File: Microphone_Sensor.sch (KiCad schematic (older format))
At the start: 29 parts, among them J4 Mic_Conn, U4 MAX4063

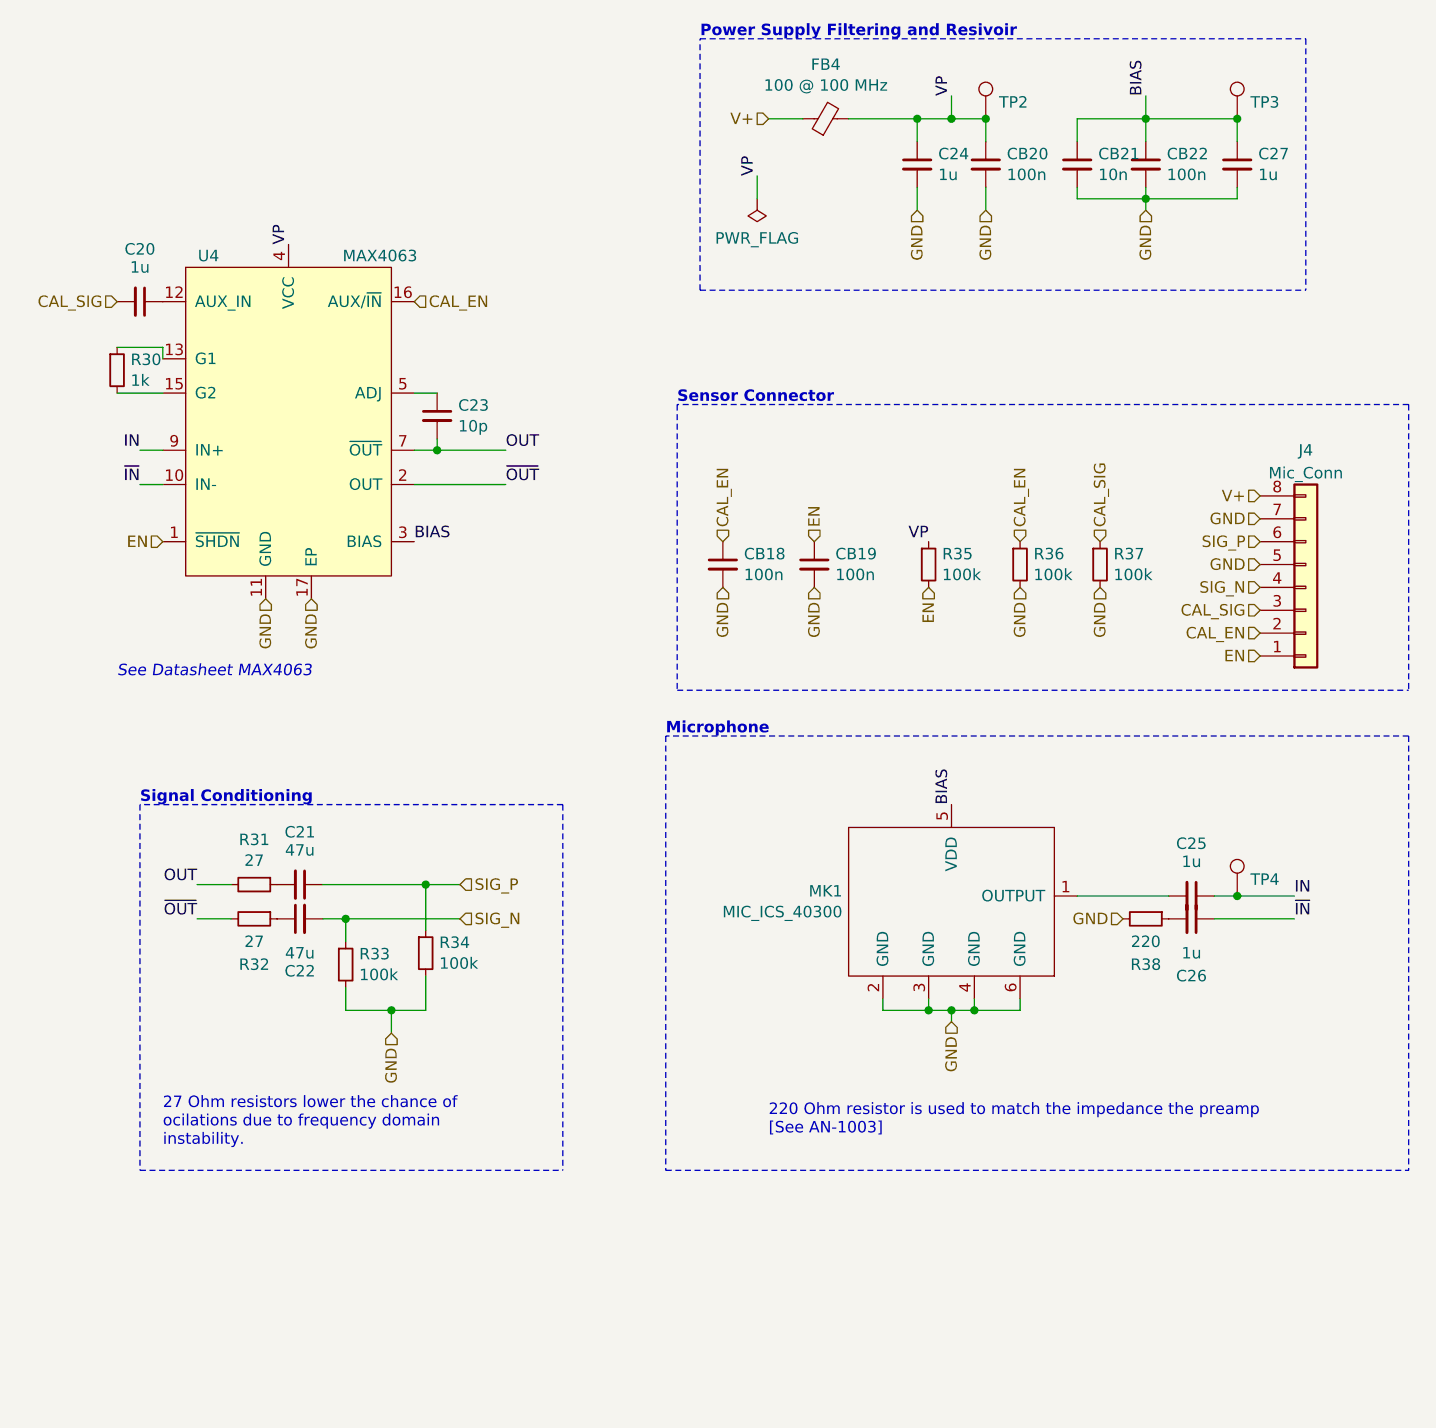
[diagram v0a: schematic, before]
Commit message: Change Sensor Connectors
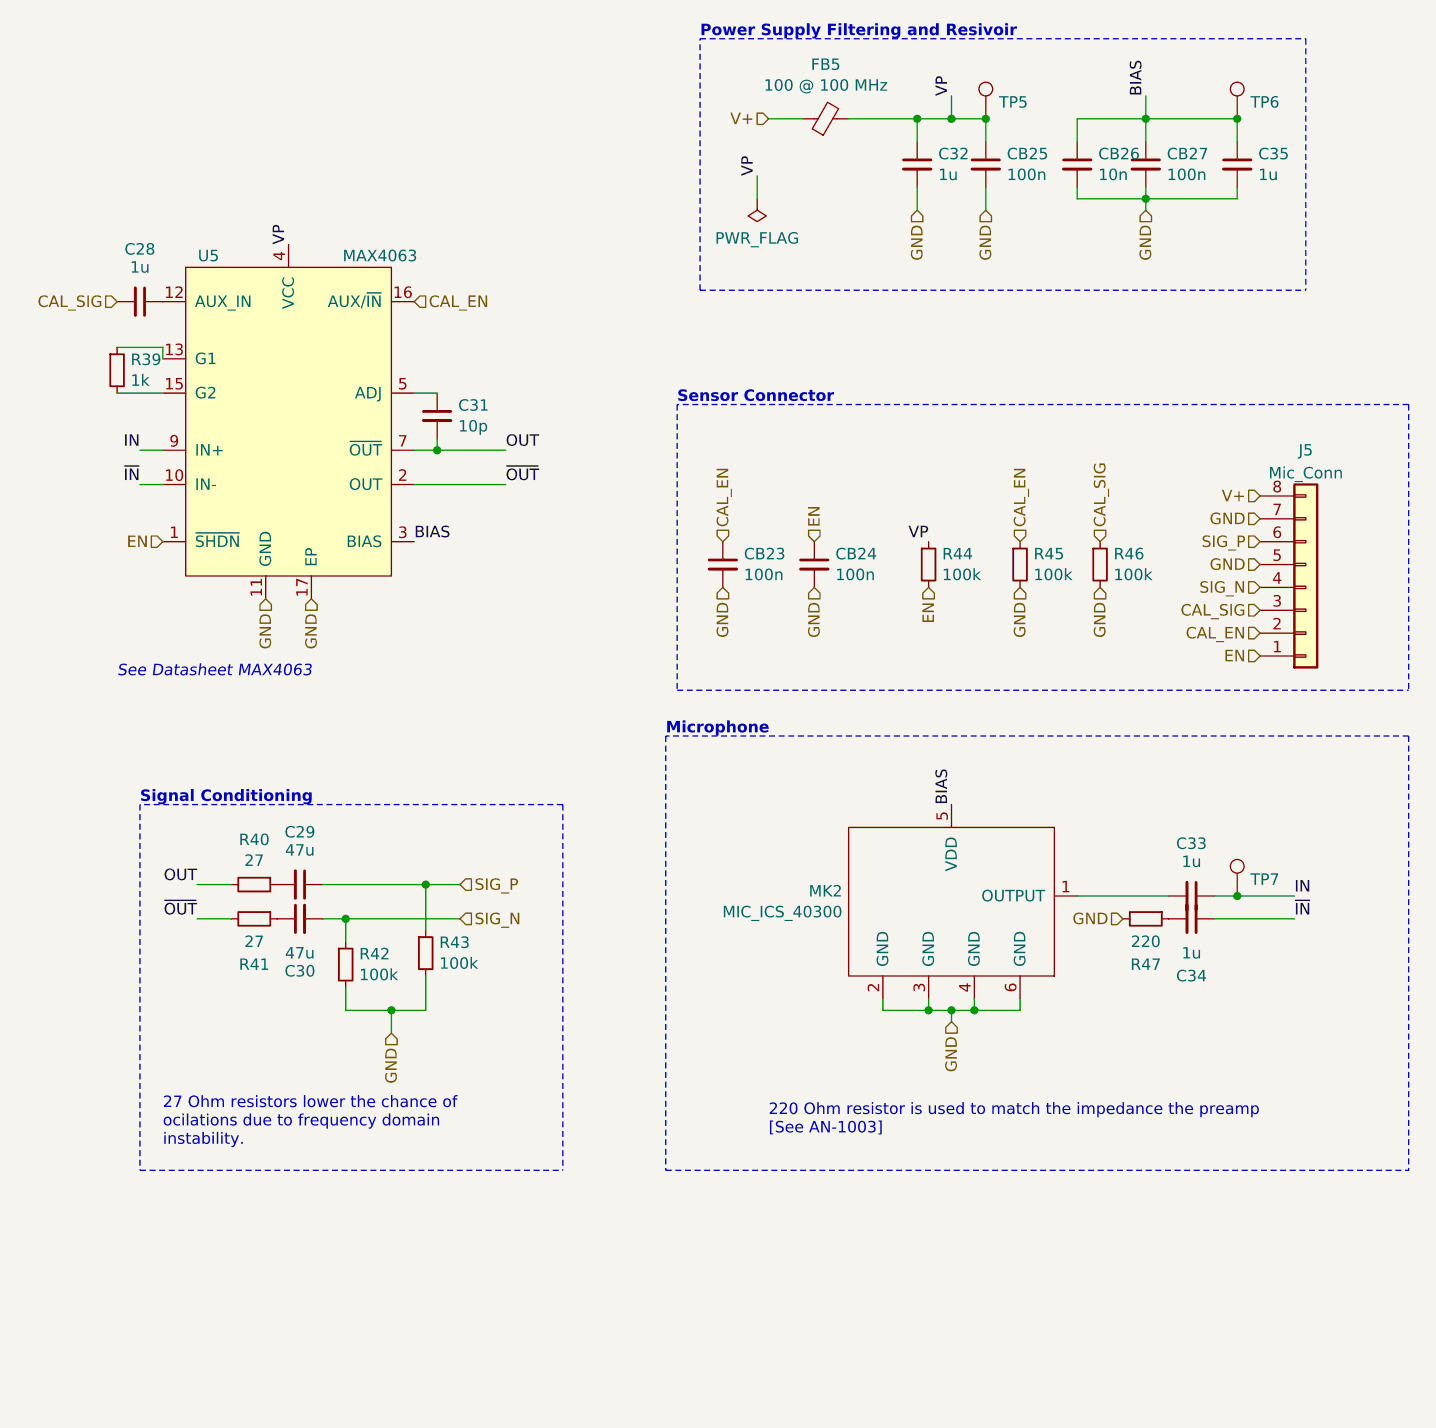
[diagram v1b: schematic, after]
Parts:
- J4: footprint Connector_Molex:Molex_PicoBlade_53047-0810_1x08_P1.25mm_Vertical -> (none); MPN 53047-0810 -> (none); Mfr. Molex -> (none)

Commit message: Setup PCB
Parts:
- J4: footprint (none) -> Connector_PinHeader_2.54mm:PinHeader_1x08_P2.54mm_Vertical
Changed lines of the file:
@@
 $Descr A4 11693 8268
 encoding utf-8
-Sheet 12 17
+Sheet 13 17
 Title "Kleinvoet"
 Date "2020-06-11"
@@
 AR Path="/5EE5ECAD/5F0013E5/5EEDE2AE" Ref="MK3"  Part="1"
 AR Path="/5EE5ECAD/5F0090C7/5EEDE2AE" Ref="MK4"  Part="1"
-F 0 "MK2" H 6123 4871 50  0000 R CNN
+F 0 "MK4" H 6123 4871 50  0000 R CNN
 F 1 "MIC_ICS_40300" H 6123 4780 50  0000 R CNN
 F 2 "grootvoet:MEMS_Mic_ICS-40300" H 6600 4750 50  0001 C CNN
@@
 AR Path="/5EE5ECAD/5F0013E5/5EEDEA2B" Ref="C56"  Part="1"
 AR Path="/5EE5ECAD/5F0090C7/5EEDEA2B" Ref="C64"  Part="1"
-F 0 "C33" V 7421 4850 50  0000 C CNN
+F 0 "C64" V 7421 4850 50  0000 C CNN
 F 1 "1u" V 7500 4850 50  0000 C CNN
 F 2 "Capacitor_SMD:C_0603_1608Metric_Pad1.05x0.95mm_HandSolder" H 7650 4850 50  0001 C CNN
@@
 AR Path="/5EE5ECAD/5F0013E5/5EEE2D96" Ref="J14"  Part="1"
 AR Path="/5EE5ECAD/5F0090C7/5EEE2D96" Ref="J15"  Part="1"
-F 0 "J5" H 8150 2900 50  0000 C CNN
+F 0 "J15" H 8150 2900 50  0000 C CNN
 F 1 "Mic_Conn" H 8150 3000 50  0000 C CNN
-F 2 "" H 8150 3500 50  0001 C CNN
+F 2 "Connector_PinHeader_2.54mm:PinHeader_1x08_P2.54mm_Vertical" H 8150 3500 50  0001 C CNN
 F 3 "~" H 8150 3500 50  0001 C CNN
 F 4 "" H 8150 3500 50  0001 C CNN "MPN"
@@
 AR Path="/5EE5ECAD/5F0013E5/5EEFDD4C" Ref="CB34"  Part="1"
 AR Path="/5EE5ECAD/5F0090C7/5EEFDD4C" Ref="CB39"  Part="1"
-F 0 "CB27" H 7542 1696 50  0000 L CNN
+F 0 "CB39" H 7542 1696 50  0000 L CNN
 F 1 "100n" H 7542 1605 50  0000 L CNN
 F 2 "Capacitor_SMD:C_0603_1608Metric_Pad1.05x0.95mm_HandSolder" H 7450 1650 50  0001 C CNN
@@
 AR Path="/5EE5ECAD/5F0013E5/5EF35019" Ref="FB9"  Part="1"
 AR Path="/5EE5ECAD/5F0090C7/5EF35019" Ref="FB10"  Part="1"
-F 0 "FB5" V 6287 1450 50  0000 C CNN
+F 0 "FB10" V 6287 1450 50  0000 C CNN
 F 1 "100 @ 100 MHz" V 6196 1450 50  0000 C CNN
 F 2 "Inductor_SMD:L_0603_1608Metric_Pad1.05x0.95mm_HandSolder" V 5980 1450 50  0001 C CNN
@@
 AR Path="/5EE5ECAD/5F0013E5/5EE150A7" Ref="R82"  Part="1"
 AR Path="/5EE5ECAD/5F0090C7/5EE150A7" Ref="R91"  Part="1"
-F 0 "R47" V 7650 4950 50  0000 C CNN
+F 0 "R91" V 7650 4950 50  0000 C CNN
 F 1 "220" V 7550 4950 50  0000 C CNN
 F 2 "Resistor_SMD:R_0603_1608Metric_Pad1.05x0.95mm_HandSolder" H 7450 4950 50  0001 C CNN
@@
 AR Path="/5EE5ECAD/5F0013E5/5EE19951" Ref="C57"  Part="1"
 AR Path="/5EE5ECAD/5F0090C7/5EE19951" Ref="C65"  Part="1"
-F 0 "C34" V 7900 4950 50  0000 C CNN
+F 0 "C65" V 7900 4950 50  0000 C CNN
 F 1 "1u" V 7800 4950 50  0000 C CNN
 F 2 "Capacitor_SMD:C_0603_1608Metric_Pad1.05x0.95mm_HandSolder" H 7650 4950 50  0001 C CNN
@@
 AR Path="/5EE5ECAD/5F0013E5/5EE3D7C0" Ref="C55"  Part="1"
 AR Path="/5EE5ECAD/5F0090C7/5EE3D7C0" Ref="C63"  Part="1"
-F 0 "C32" H 6542 1696 50  0000 L CNN
+F 0 "C63" H 6542 1696 50  0000 L CNN
 F 1 "1u" H 6542 1605 50  0000 L CNN
 F 2 "Capacitor_SMD:C_0603_1608Metric_Pad1.05x0.95mm_HandSolder" H 6450 1650 50  0001 C CNN
@@
 AR Path="/5EE5ECAD/5F0013E5/5EE4D182" Ref="C58"  Part="1"
 AR Path="/5EE5ECAD/5F0090C7/5EE4D182" Ref="C66"  Part="1"
-F 0 "C35" H 7942 1696 50  0000 L CNN
+F 0 "C66" H 7942 1696 50  0000 L CNN
 F 1 "1u" H 7942 1605 50  0000 L CNN
 F 2 "Capacitor_SMD:C_0603_1608Metric_Pad1.05x0.95mm_HandSolder" H 7850 1650 50  0001 C CNN
@@
 AR Path="/5EE5ECAD/5F0013E5/5EE3C381" Ref="CB32"  Part="1"
 AR Path="/5EE5ECAD/5F0090C7/5EE3C381" Ref="CB37"  Part="1"
-F 0 "CB25" H 6842 1696 50  0000 L CNN
+F 0 "CB37" H 6842 1696 50  0000 L CNN
 F 1 "100n" H 6842 1605 50  0000 L CNN
 F 2 "Capacitor_SMD:C_0603_1608Metric_Pad1.05x0.95mm_HandSolder" H 6750 1650 50  0001 C CNN
@@
 AR Path="/5EE5ECAD/5F0013E5/5EE68FFE" Ref="R77"  Part="1"
 AR Path="/5EE5ECAD/5F0090C7/5EE68FFE" Ref="R86"  Part="1"
-F 0 "R42" H 4009 5196 50  0000 L CNN
+F 0 "R86" H 4009 5196 50  0000 L CNN
 F 1 "100k" H 4009 5105 50  0000 L CNN
 F 2 "Resistor_SMD:R_0603_1608Metric_Pad1.05x0.95mm_HandSolder" H 3950 5150 50  0001 C CNN
@@
 AR Path="/5EE5ECAD/5F0013E5/5EE699A6" Ref="R78"  Part="1"
 AR Path="/5EE5ECAD/5F0090C7/5EE699A6" Ref="R87"  Part="1"
-F 0 "R43" H 4359 5146 50  0000 L CNN
+F 0 "R87" H 4359 5146 50  0000 L CNN
 F 1 "100k" H 4359 5055 50  0000 L CNN
 F 2 "Resistor_SMD:R_0603_1608Metric_Pad1.05x0.95mm_HandSolder" H 4300 5100 50  0001 C CNN
@@
 AR Path="/5EE5ECAD/5F0013E5/5EE840BE" Ref="R75"  Part="1"
 AR Path="/5EE5ECAD/5F0090C7/5EE840BE" Ref="R84"  Part="1"
-F 0 "R40" V 3354 4800 50  0000 C CNN
+F 0 "R84" V 3354 4800 50  0000 C CNN
 F 1 "27" V 3445 4800 50  0000 C CNN
 F 2 "Resistor_SMD:R_0603_1608Metric_Pad1.05x0.95mm_HandSolder" H 3550 4800 50  0001 C CNN
@@
 AR Path="/5EE5ECAD/5F0013E5/5EE845A7" Ref="R76"  Part="1"
 AR Path="/5EE5ECAD/5F0090C7/5EE845A7" Ref="R85"  Part="1"
-F 0 "R41" V 3750 4950 50  0000 C CNN
+F 0 "R85" V 3750 4950 50  0000 C CNN
 F 1 "27" V 3650 4950 50  0000 C CNN
 F 2 "Resistor_SMD:R_0603_1608Metric_Pad1.05x0.95mm_HandSolder" H 3550 4950 50  0001 C CNN
@@
 AR Path="/5EE5ECAD/5F0013E5/5EE94347" Ref="C52"  Part="1"
 AR Path="/5EE5ECAD/5F0090C7/5EE94347" Ref="C60"  Part="1"
-F 0 "C29" V 3521 4800 50  0000 C CNN
+F 0 "C60" V 3521 4800 50  0000 C CNN
 F 1 "47u" V 3600 4800 50  0000 C CNN
 F 2 "Capacitor_SMD:C_1206_3216Metric_Pad1.42x1.75mm_HandSolder" H 3750 4800 50  0001 C CNN
@@
 AR Path="/5EE5ECAD/5F0013E5/5EEE5C9C" Ref="CB33"  Part="1"
 AR Path="/5EE5ECAD/5F0090C7/5EEE5C9C" Ref="CB38"  Part="1"
-F 0 "CB26" H 7242 1696 50  0000 L CNN
+F 0 "CB38" H 7242 1696 50  0000 L CNN
 F 1 "10n" H 7242 1605 50  0000 L CNN
 F 2 "Capacitor_SMD:C_0603_1608Metric_Pad1.05x0.95mm_HandSolder" H 7150 1650 50  0001 C CNN
@@
 AR Path="/5EE5ECAD/5F0013E5/5F1831E4" Ref="#FLG0102"  Part="1"
 AR Path="/5EE5ECAD/5F0090C7/5F1831E4" Ref="#FLG0103"  Part="1"
-F 0 "#FLG0101" H 5750 1875 50  0001 C CNN
+F 0 "#FLG0103" H 5750 1875 50  0001 C CNN
 F 1 "PWR_FLAG" H 5750 1973 50  0000 C CNN
 F 2 "" H 5750 1800 50  0001 C CNN
@@
 AR Path="/5EE5ECAD/5F0013E5/5F1F0F4E" Ref="C53"  Part="1"
 AR Path="/5EE5ECAD/5F0090C7/5F1F0F4E" Ref="C61"  Part="1"
-F 0 "C30" V 3521 4950 50  0000 C CNN
+F 0 "C61" V 3521 4950 50  0000 C CNN
 F 1 "47u" V 3600 4950 50  0000 C CNN
 F 2 "Capacitor_SMD:C_1206_3216Metric_Pad1.42x1.75mm_HandSolder" H 3750 4950 50  0001 C CNN
@@
 AR Path="/5EE5ECAD/5F0013E5/5F1557AF" Ref="TP13"  Part="1"
 AR Path="/5EE5ECAD/5F0090C7/5F1557AF" Ref="TP16"  Part="1"
-F 0 "TP7" H 7908 4922 50  0000 L CNN
+F 0 "TP16" H 7908 4922 50  0000 L CNN
 F 1 "TestPoint" H 7908 4877 50  0001 L CNN
 F 2 "TestPoint:TestPoint_Pad_D1.0mm" H 8050 4850 50  0001 C CNN
@@
 AR Path="/5EE5ECAD/5F0013E5/5F157F47" Ref="TP11"  Part="1"
 AR Path="/5EE5ECAD/5F0090C7/5F157F47" Ref="TP14"  Part="1"
-F 0 "TP5" H 6808 1522 50  0000 L CNN
+F 0 "TP14" H 6808 1522 50  0000 L CNN
 F 1 "TestPoint" H 6808 1477 50  0001 L CNN
 F 2 "TestPoint:TestPoint_Pad_D1.0mm" H 6950 1450 50  0001 C CNN
@@
 AR Path="/5EE5ECAD/5F0013E5/5F15842C" Ref="TP12"  Part="1"
 AR Path="/5EE5ECAD/5F0090C7/5F15842C" Ref="TP15"  Part="1"
-F 0 "TP6" H 7908 1522 50  0000 L CNN
+F 0 "TP15" H 7908 1522 50  0000 L CNN
 F 1 "TestPoint" H 7908 1477 50  0001 L CNN
 F 2 "TestPoint:TestPoint_Pad_D1.0mm" H 8050 1450 50  0001 C CNN
@@
 AR Path="/5EE5ECAD/5F0013E5/5F061452" Ref="C54"  Part="1"
 AR Path="/5EE5ECAD/5F0090C7/5F061452" Ref="C62"  Part="1"
-F 0 "C31" H 4442 2796 50  0000 L CNN
+F 0 "C62" H 4442 2796 50  0000 L CNN
 F 1 "10p" H 4442 2705 50  0000 L CNN
 F 2 "Capacitor_SMD:C_0603_1608Metric_Pad1.05x0.95mm_HandSolder" H 4350 2750 50  0001 C CNN
@@
 AR Path="/5EE5ECAD/5F0013E5/5F059C63" Ref="U10"  Part="1"
 AR Path="/5EE5ECAD/5F0090C7/5F059C63" Ref="U11"  Part="1"
-F 0 "U5" H 3350 3450 50  0000 C CNN
+F 0 "U11" H 3350 3450 50  0000 C CNN
 F 1 "MAX4063" H 4100 3450 50  0000 C CNN
 F 2 "grootvoet:TQFN-16-T1644++4" H 2250 3550 50  0001 C CNN
@@
 AR Path="/5EE5ECAD/5F0013E5/5F08A647" Ref="R74"  Part="1"
 AR Path="/5EE5ECAD/5F0090C7/5F08A647" Ref="R83"  Part="1"
-F 0 "R39" H 3009 2596 50  0000 L CNN
+F 0 "R83" H 3009 2596 50  0000 L CNN
 F 1 "1k" H 3009 2505 50  0000 L CNN
 F 2 "Resistor_SMD:R_0603_1608Metric_Pad1.05x0.95mm_HandSolder" H 2950 2550 50  0001 C CNN
@@
 AR Path="/5EE5ECAD/5F0013E5/5F098CC5" Ref="C51"  Part="1"
 AR Path="/5EE5ECAD/5F0090C7/5F098CC5" Ref="C59"  Part="1"
-F 0 "C28" V 2821 2250 50  0000 C CNN
+F 0 "C59" V 2821 2250 50  0000 C CNN
 F 1 "1u" V 2900 2250 50  0000 C CNN
 F 2 "Capacitor_SMD:C_0603_1608Metric_Pad1.05x0.95mm_HandSolder" H 3050 2250 50  0001 C CNN
@@
 AR Path="/5EE5ECAD/5F0013E5/5F0C0D18" Ref="R79"  Part="1"
 AR Path="/5EE5ECAD/5F0090C7/5F0C0D18" Ref="R88"  Part="1"
-F 0 "R44" H 6559 3446 50  0000 L CNN
+F 0 "R88" H 6559 3446 50  0000 L CNN
 F 1 "100k" H 6559 3355 50  0000 L CNN
 F 2 "Resistor_SMD:R_0603_1608Metric_Pad1.05x0.95mm_HandSolder" H 6500 3400 50  0001 C CNN
@@
 AR Path="/5EE5ECAD/5F0013E5/5F0C11FF" Ref="R80"  Part="1"
 AR Path="/5EE5ECAD/5F0090C7/5F0C11FF" Ref="R89"  Part="1"
-F 0 "R45" H 6959 3446 50  0000 L CNN
+F 0 "R89" H 6959 3446 50  0000 L CNN
 F 1 "100k" H 6959 3355 50  0000 L CNN
 F 2 "Resistor_SMD:R_0603_1608Metric_Pad1.05x0.95mm_HandSolder" H 6900 3400 50  0001 C CNN
@@
 AR Path="/5EE5ECAD/5F0013E5/5F0C14A4" Ref="R81"  Part="1"
 AR Path="/5EE5ECAD/5F0090C7/5F0C14A4" Ref="R90"  Part="1"
-F 0 "R46" H 7309 3446 50  0000 L CNN
+F 0 "R90" H 7309 3446 50  0000 L CNN
 F 1 "100k" H 7309 3355 50  0000 L CNN
 F 2 "Resistor_SMD:R_0603_1608Metric_Pad1.05x0.95mm_HandSolder" H 7250 3400 50  0001 C CNN
@@
 AR Path="/5EE5ECAD/5F0013E5/5F05E979" Ref="CB30"  Part="1"
 AR Path="/5EE5ECAD/5F0090C7/5F05E979" Ref="CB35"  Part="1"
-F 0 "CB23" H 5692 3446 50  0000 L CNN
+F 0 "CB35" H 5692 3446 50  0000 L CNN
 F 1 "100n" H 5692 3355 50  0000 L CNN
 F 2 "Capacitor_SMD:C_0603_1608Metric_Pad1.05x0.95mm_HandSolder" H 5600 3400 50  0001 C CNN
@@
 AR Path="/5EE5ECAD/5F0013E5/5F05E4AA" Ref="CB31"  Part="1"
 AR Path="/5EE5ECAD/5F0090C7/5F05E4AA" Ref="CB36"  Part="1"
-F 0 "CB24" H 6092 3446 50  0000 L CNN
+F 0 "CB36" H 6092 3446 50  0000 L CNN
 F 1 "100n" H 6092 3355 50  0000 L CNN
 F 2 "Capacitor_SMD:C_0603_1608Metric_Pad1.05x0.95mm_HandSolder" H 6000 3400 50  0001 C CNN

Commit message: PCB Layout Checkpoint
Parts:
- added H5, H6: MountingHole, MountingHole:MountingHole_2.7mm_M2.5_DIN965_Pad, symbol Mechanical:MountingHole
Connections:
- net CAL_EN: now also J4.6 (Pin_6); no longer J4.2 (Pin_2)
- net CAL_SIG: now also J4.7 (Pin_7); no longer J4.3 (Pin_3)
- net EN: now also J4.5 (Pin_5); no longer J4.1 (Pin_1)
- net GND: now also J4.3 (Pin_3), J4.8 (Pin_8); no longer J4.5 (Pin_5), J4.7 (Pin_7)
- net IN: now also C26.1; no longer C25.1, TP4.1
- net SIG_N: now also J4.2 (Pin_2); no longer J4.4 (Pin_4)
- net SIG_P: now also J4.1 (Pin_1); no longer J4.6 (Pin_6)
- net V+: now also J4.4 (Pin_4); no longer J4.8 (Pin_8)
- net ~IN: now also C25.1, TP4.1; no longer C26.1
- net OUT renamed OUT_P
- net ~OUT renamed OUT_N
